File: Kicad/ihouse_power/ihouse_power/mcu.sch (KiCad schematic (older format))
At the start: 75 parts, among them J13 RC, J3 Conn_01x20, J4 Conn_01x20, M1 stm32f1_module, U10 MAX232, U11 L7805, U6 EL814, U7 EL814, U8 EL814, U9 24LC32

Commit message: schemos, pcb ruosimas
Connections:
- net labels added: HUM1_AI, HUM2_AI, HUM3_AI, NEXRX, NEXTX, OPTIC_AI, RSRCEN, TEMP_AI
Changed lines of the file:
@@
 EESchema Schematic File Version 4
 LIBS:ihouse_power-cache
-EELAYER 29 0
+EELAYER 26 0
 EELAYER END
 $Descr A3 16535 11693
@@
 	7150 5400 7600 5400
 Text HLabel 7150 6100 0    50   Input ~ 0
+TBRX
+Text HLabel 7150 6200 0    50   Output ~ 0
 TBTX
-Text HLabel 7150 6200 0    50   Output ~ 0
-TBRX
 Text HLabel 9000 6000 2    50   Output ~ 0
 ~TBCMD
@@
 Text Label 9000 6500 2    50   ~ 0
 C15
-Text Label 7150 5400 0    50   ~ 0
-A2
-Text Label 7150 5500 0    50   ~ 0
-A3
-Text Label 7150 5900 0    50   ~ 0
-A7
 Text Label 9000 5500 2    50   ~ 0
 B10
@@
 A0
 Text Label 7150 5200 0    50   ~ 0
-A0
-Text Label 7150 5300 0    50   ~ 0
-A1
-Text Label 7150 5600 0    50   ~ 0
-A4
-Text Label 7150 5700 0    50   ~ 0
-A5
-Text Label 7150 5800 0    50   ~ 0
-A6
+OPTIC_AI
 $Comp
 L Regulator_Linear:L7805 U11
@@
 	5400 1450 6000 1450
 Text Label 4100 4400 2    50   ~ 0
-A2
+NEXRX
 Text Label 4100 4700 2    50   ~ 0
-A3
-Text Label 3100 7700 2    50   ~ 0
-A0
+NEXTX
 Text Label 3100 8250 2    50   ~ 0
-A1
+HUM1_AI
 Text Label 3100 8800 2    50   ~ 0
-A4
+HUM2_AI
 Text Label 3100 9350 2    50   ~ 0
-A5
+HUM3_AI
 Text Label 3100 9900 2    50   ~ 0
-A6
+TEMP_AI
 Text Label 6000 1450 2    50   ~ 0
 A7
@@
 Wire Wire Line
 	6150 4950 6550 4950
+Text Label 3100 7700 2    50   ~ 0
+OPTIC_AI
+Text Label 7150 5300 0    50   ~ 0
+HUM1_AI
+Text Label 7150 5600 0    50   ~ 0
+HUM2_AI
+Text Label 7150 5700 0    50   ~ 0
+HUM3_AI
+Text Label 7150 5800 0    50   ~ 0
+TEMP_AI
+Text Label 7150 5900 0    50   ~ 0
+VLINE
+Text Label 7150 5500 0    50   ~ 0
+NEXTX
+Text Label 7150 5400 0    50   ~ 0
+NEXRX
+Text Label 2200 4800 0    50   ~ 0
+RSRCEN
 $EndSCHEMATC

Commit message: schemos ir pcb plokstes ruosimas
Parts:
- removed J13: RC, rj45_vertical_shelded:RJ45_Vertical, symbol Connector:8P8C
- added C28, C29: C, Capacitor_SMD:C_1206_3216Metric_Pad1.42x1.75mm_HandSolder, symbol Device:C
- added J13: RJ33_Shielded, rj45_vertical_shelded:RJ45_Vertical, symbol Connector:RJ33_Shielded
- added Q1, Q2, Q3, Q4: Q_NMOS_DGS, symbol Device:Q_NMOS_DGS
- added R12, R13, R34, R35, R36, R37: 47k, Resistor_SMD:R_1206_3216Metric, symbol Device:R
- added U12, U13: IR2101, Package_SO:SOIC-8_3.9x4.9mm_P1.27mm, symbol Driver_FET:IR2101
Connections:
- net labels added: 5VDC1, VB
- wire segments 348 -> 418

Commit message: schemos ir pcb ruosimas
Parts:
- removed C28, C29: C, Capacitor_SMD:C_1206_3216Metric_Pad1.42x1.75mm_HandSolder, symbol Device:C
- removed Q1, Q2, Q3, Q4: Q_NMOS_DGS, symbol Device:Q_NMOS_DGS
- removed U12, U13: IR2101, Package_SO:SOIC-8_3.9x4.9mm_P1.27mm, symbol Driver_FET:IR2101
- added BZ1: Buzzer, symbol Device:Buzzer
- added C28, C29, C30: CP, Capacitor_THT:CP_Radial_D8.0mm_P3.50mm, symbol Device:CP
- added D11: GBU6A, Diode_THT:Diode_Bridge_Vishay_GBU, symbol Diode_Bridge:GBU6A
- added D12: BAS32, Diode_SMD:D_MiniMELF, symbol Device:D
- added F3, F4, F5, F6: 33V/3A, Fuse:Fuse_2920_7451Metric_Pad2.10x5.45mm_HandSolder, symbol Device:Polyfuse
- added J20: Conn_02x05_Top_Bottom, Connector_Molex:Molex_Mini-Fit_Jr_5566-10A_2x05_P4.20mm_Vertical, symbol Connector_Generic:Conn_02x05_Top_Bottom
- added Q1, Q2, Q3, Q4: IRF7403, Package_SO:SOIC-8_3.9x4.9mm_P1.27mm, symbol Transistor_FET:IRF7403
- added Q5: BC847, Package_TO_SOT_SMD:SOT-23, symbol Transistor_BJT:BC847
- added R38, R39, R40, R41: 100, Resistor_SMD:R_0805_2012Metric_Pad1.15x1.40mm_HandSolder, symbol Device:R
- added R42, R43, R44, R45, R46, R47: 10k, Resistor_SMD:R_0805_2012Metric_Pad1.15x1.40mm_HandSolder, symbol Device:R
- added R48: 47, Resistor_SMD:R_1206_3216Metric, symbol Device:R
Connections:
- net labels added: BUZMN, BUZPL, BUZZ, VS
- wire segments 418 -> 463

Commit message: schemos ir pcb paruosimas
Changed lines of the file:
@@
 EESchema Schematic File Version 4
 LIBS:ihouse_power-cache
-EELAYER 26 0
+EELAYER 29 0
 EELAYER END
 $Descr A3 16535 11693
@@
 BUZMN
 Wire Wire Line
-	9300 10750 8900 10750
-Wire Wire Line
 	8900 8650 8900 9350
 Wire Wire Line
@@
 	9700 10750 10050 10750
 Wire Wire Line
-	9300 10750 9700 10750
+	8900 10750 9700 10750
 $EndSCHEMATC

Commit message: schemos ir pcb ruosimas
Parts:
- R12, R13, R14, R15, R16, R17, R18, R19, R20, R21, R22, R34, R35, R36, R37, R5, R6, R7: value 47k -> 22k
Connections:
- net B10 is gone; now on net LPULSE1: J4.15 (Pin_15), M1.15 (B10)
- net B11 is gone; now on net LPULSE2: J4.16 (Pin_16), M1.16 (B11)
- net B3 is gone; now on net LPULSE: J3.10 (Pin_10), M1.30 (B3)
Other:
- moved on the sheet: BT1, C28, C29, C30, D11, F3, F4, F5, F6, J20, M1, Q1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

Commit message: prideta schema ir pcb lcd ekrano rs232 draiverio
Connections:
- net RSRCEN is gone; now on net RCEN: J13.4, U10.8 (R2IN)
- net RSRX renamed RS2
- net RSTX renamed RS1
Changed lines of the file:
@@
 	3150 3350 3150 3400
 Text Label 2300 4400 0    50   ~ 0
-RSTX
+RS1
 Text Label 2300 4700 0    50   ~ 0
-RSRX
+RS2
 Wire Wire Line
 	1950 4050 2200 4050
@@
 NEXRX
 Text Label 2200 4800 0    50   ~ 0
-RSRCEN
+RCEN
 Text HLabel 4350 2250 2    50   Output ~ 0
 5VDC1

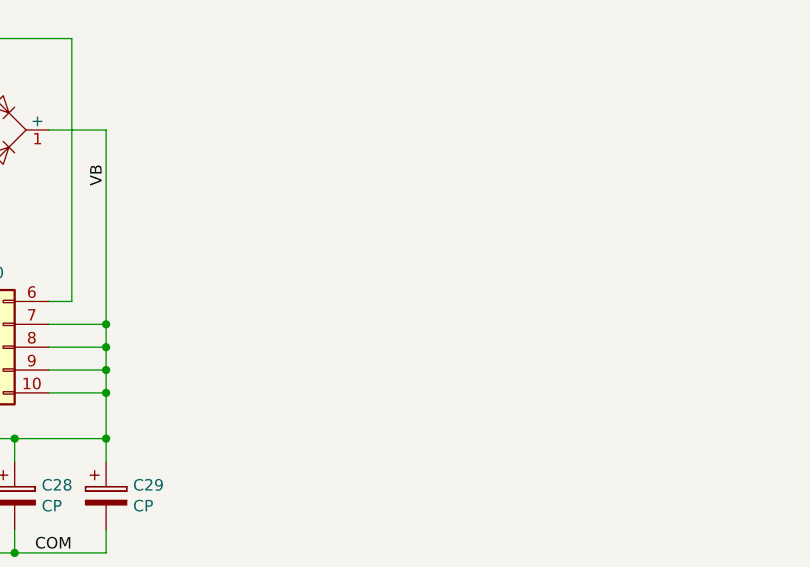
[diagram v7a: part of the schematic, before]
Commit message: i2c modulio tvarkymas, ds1307 modulio tvarkymas. ds1307 veikia
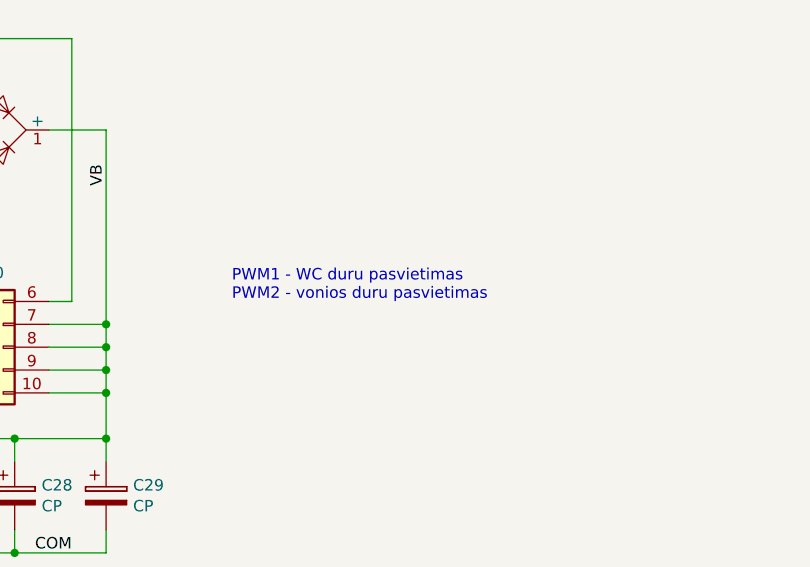
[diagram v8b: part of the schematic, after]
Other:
- note added: "PWM1 - WC duru pasvietimas\nPWM2 - vonios duru pasvietimas"
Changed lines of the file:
@@
 Text HLabel 8500 5250 2    50   Input ~ 0
 LPULSE2
+Text Notes 10300 9200 0    50   ~ 0
+PWM1 - WC duru pasvietimas\nPWM2 - vonios duru pasvietimas
 $EndSCHEMATC
